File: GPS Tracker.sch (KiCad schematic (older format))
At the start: 8 parts

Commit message: Finished Schematic, may need power supply fixes
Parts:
- added C? (x2): 22pf, symbol Device:C
- added C?: 0.1uF, symbol Device:C
- added C?: 4.7uF, symbol Device:C
- added C?: 10nF, symbol Device:C
- added C?: 1uF, symbol Device:C
- added D?: PWR, symbol Device:LED
- added D?: STATUS, symbol Device:LED
- added D?: LOCK, symbol Device:LED
- added D?: RADIO, symbol Device:LED
- added J?: BAT, symbol Connector:Conn_01x02_Male
- added J?: JTAG, symbol Connector:Conn_01x04_Male
- added J?: u.fl Connector, digikey-footprints:Molex_734120114_UMC_RF_CONN_Vertical, symbol dk_Coaxial-Connectors-RF:0734120114
- added JP?: BOOT0, symbol Jumper:SolderJumper_3_Bridged12
- added Q?: TSM2309, symbol TSM2309:TSM2309
- added R? (x7): 10K, symbol Device:R
- added Y?: 8MHz, symbol Device:Crystal
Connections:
- net +3V3: now also C?.1, C?.1, C?.1, C?.1, D?.2 (A), D?.2 (A), D?.2 (A), D?.2 (A), J?.1 (Pin_1), JP?.3 (B), R?.1, R?.2
- net GND: now also C?.1, C?.1, C?.2, C?.2, C?.2, C?.2, J?.1, J?.1 (Pin_1), J?.4 (Pin_4), JP?.1 (A), Q?.1 (G), R?.1
- net GPS_RX: now also U?.9 (PA3)
- net GPS_TX: now also U?.8 (PA2)
- net MISO: now also U?.12 (PA6)
- net MOSI: now also U?.13 (PA7)
- net SCK: now also U?.11 (PA5)
- net USB_DM: now also U?.17 (PA9/PA11)
- net USB_DP: now also U?.18 (PA10/PA12)
- net at U?.1 (BOOT0): now also R?.1
- net RADIO: now reaches U?.10 (PA4)
- net RADIO: now also R?.1
- net SWDIO: now reaches U?.19 (PA13)
- net SWDIO: now also J?.2 (Pin_2)
- net OSC_IN: now reaches U?.2 (PF0)
- net OSC_IN: now also C?.2, Y?.1
- net SWCLK: now reaches U?.20 (PA14)
- net SWCLK: now also J?.3 (Pin_3)
- net OSC_OUT: now reaches U?.3 (PF1)
- net OSC_OUT: now also C?.2, Y?.2
- net at U?.4 (NRST): now also R?.2
- net STATUS: now reaches U?.6 (PA0)
- net STATUS: now also R?.1
- net LOCK: now reaches U?.7 (PA1)
- net LOCK: now also R?.1
- net at U?.6 (RESET): now also R?.1
- net at U?.9 (ANT): now also J?.2
- new net: JP?.2 (C), R?.2
- new net: D?.1 (K), R?.2 (x4)
- new net BAT_RAW+: J?.2 (Pin_2), Q?.3 (D)
- new net V_IN: Q?.2 (S)
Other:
- note added: "Reverse Polarity Protection"
- note added: "Status LEDs"
- note added: "VDD Decoupling"
- note added: "VDDA Decoupling"
- moved on the sheet: U?

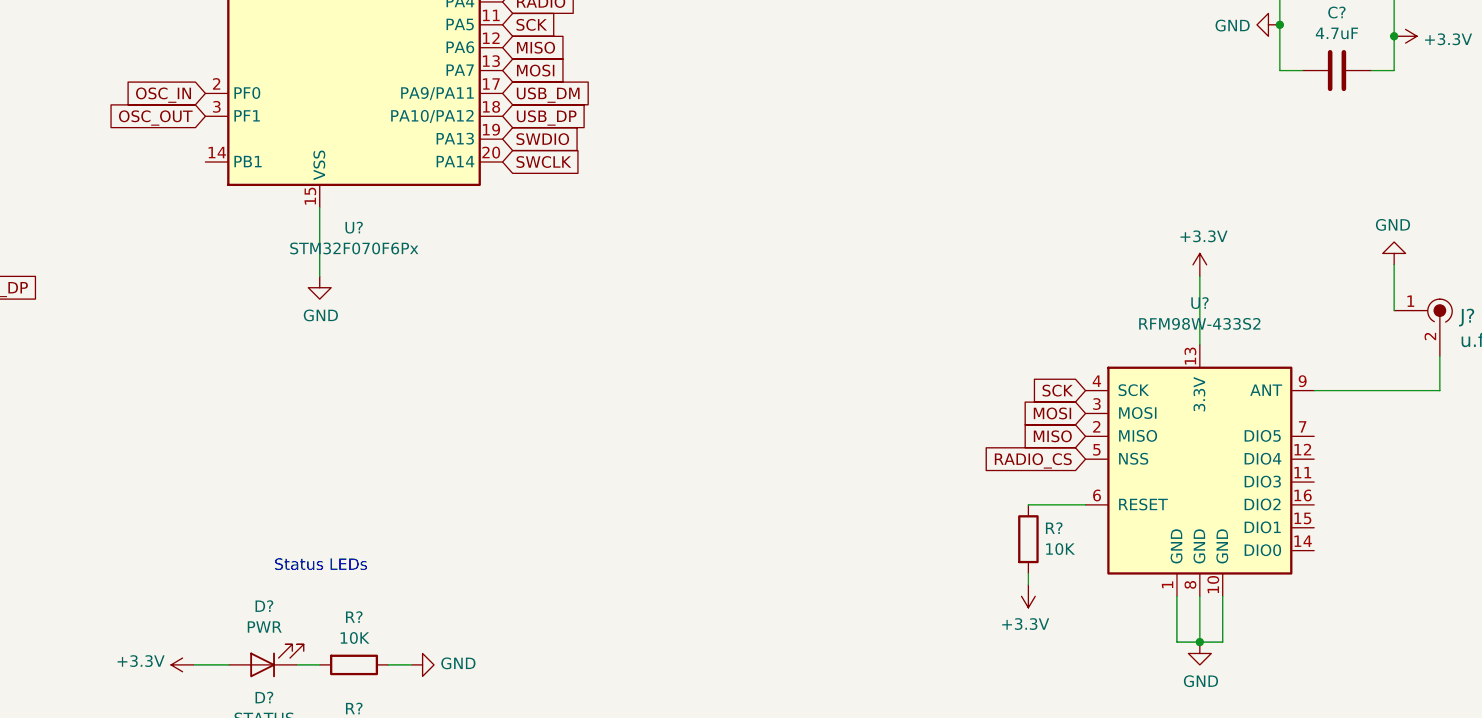
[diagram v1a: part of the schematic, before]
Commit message: Fixed unconnected pins
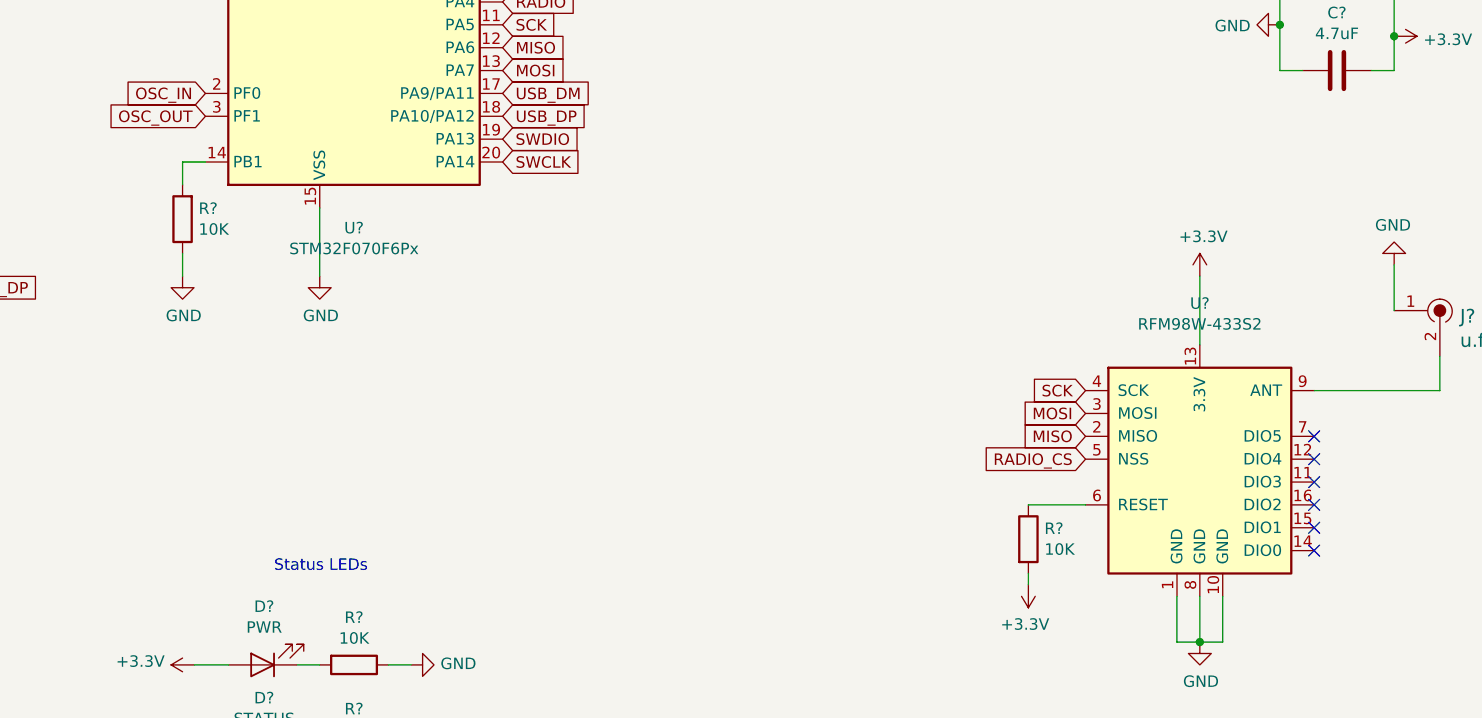
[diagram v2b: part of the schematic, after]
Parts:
- added R?: 10K, symbol Device:R
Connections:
- net GND: now also R?.1
- net at U?.14 (PB1): now also R?.2
- no-connect marks 1 -> 7
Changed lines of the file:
@@
 Text Notes 5250 5400 0    50   ~ 0
 Status LEDs
+$Comp
+L Device:R R?
+U 1 1 5E4267A8
+P 4850 3850
+F 0 "R?" H 4780 3804 50  0000 R CNN
+F 1 "10K" H 4780 3895 50  0000 R CNN
+F 2 "" V 4780 3850 50  0001 C CNN
+F 3 "~" H 4850 3850 50  0001 C CNN
+	1    4850 3850
+	-1   0    0    1
+$EndComp
+$Comp
+L power:GND #PWR?
+U 1 1 5E429908
+P 4850 4100
+F 0 "#PWR?" H 4850 3850 50  0001 C CNN
+F 1 "GND" H 4855 3927 50  0000 C CNN
+F 2 "" H 4850 4100 50  0001 C CNN
+F 3 "" H 4850 4100 50  0001 C CNN
+	1    4850 4100
+	1    0    0    -1
+$EndComp
+Wire Wire Line
+	4850 4100 4850 4000
+Wire Wire Line
+	4850 3700 4850 3600
+Wire Wire Line
+	4850 3600 4950 3600
+NoConn ~ 9800 4800
+NoConn ~ 9800 4900
+NoConn ~ 9800 5000
+NoConn ~ 9800 5100
+NoConn ~ 9800 5200
+NoConn ~ 9800 5300
 $EndSCHEMATC
